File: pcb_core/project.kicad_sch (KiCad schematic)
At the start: 53 parts, among them IC4 TCA9548APWR, J1 Conn_01x02, J19 Conn_02x02_Counter_Clockwise, J2 1725656, J20 PCBConnector, J21 PCBConnector, J22 PCBConnector, J23 PCBConnector, J25 PCBConnector, J27 PCBConnector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

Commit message: Add missing PWR_FLAGs
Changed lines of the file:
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@@
 	)
 	(junction
+		(at 405.13 387.35)
+		(diameter 0)
+		(color 0 0 0 0)
+	)
+	(junction
 		(at 102.87 25.4)
 		(diameter 0)
@@
 	)
 	(junction
+		(at 405.13 389.89)
+		(diameter 0)
+		(color 0 0 0 0)
+	)
+	(junction
 		(at 143.51 349.25)
 		(diameter 0)
@@
 	(wire
 		(pts
+			(xy 405.13 389.89) (xy 414.02 389.89)
+		)
+		(stroke
+			(width 0)
+			(type default)
+		)
+	)
+	(wire
+		(pts
 			(xy 386.08 365.76) (xy 382.27 365.76)
 		)
@@
 	(wire
 		(pts
-			(xy 397.51 389.89) (xy 414.02 389.89)
+			(xy 397.51 389.89) (xy 405.13 389.89)
 		)
 		(stroke
@@
 	(wire
 		(pts
+			(xy 405.13 387.35) (xy 414.02 387.35)
+		)
+		(stroke
+			(width 0)
+			(type default)
+		)
+	)
+	(wire
+		(pts
 			(xy 176.53 116.84) (xy 176.53 118.11)
 		)
@@
 	(wire
 		(pts
-			(xy 383.54 387.35) (xy 414.02 387.35)
+			(xy 383.54 387.35) (xy 405.13 387.35)
 		)
 		(stroke
@@
 		)
 	)
-	(label "VDD33"
-		(at 180.34 31.75 0)
-		(fields_autoplaced yes)
-		(effects
-			(font
-				(size 1.27 1.27)
-			)
-			(justify left bottom)
-		)
-	)
 	(label "ESP32_TX"
 		(at 167.64 45.72 0)
@@
 	)
 	(symbol
+		(lib_id "power:PWR_FLAG")
+		(at 405.13 387.35 0)
+		(unit 1)
+		(exclude_from_sim no)
+		(in_bom yes)
+		(on_board yes)
+		(dnp no)
+		(fields_autoplaced yes)
+		(property "Reference" "#FLG01"
+			(at 405.13 385.445 0)
+			(effects
+				(font
+					(size 1.27 1.27)
+				)
+				(hide yes)
+			)
+		)
+		(property "Value" "PWR_FLAG"
+			(at 405.13 382.27 0)
+			(effects
+				(font
+					(size 1.27 1.27)
+				)
+			)
+		)
+		(property "Footprint" ""
+			(at 405.13 387.35 0)
+			(effects
+				(font
+					(size 1.27 1.27)
+				)
+				(hide yes)
+			)
+		)
+		(property "Datasheet" "~"
+			(at 405.13 387.35 0)
+			(effects
+				(font
+					(size 1.27 1.27)
+				)
+				(hide yes)
+			)
+		)
+		(property "Description" "Special symbol for telling ERC where power comes from"
+			(at 405.13 387.35 0)
+			(effects
+				(font
+					(size 1.27 1.27)
+				)
+				(hide yes)
+			)
+		)
+		(pin "1"
+		)
+		(instances
+			(project "project"
+				(path "/97ee99f6-6664-45d1-b5d6-247aaf34e934"
+					(reference "#FLG01")
+					(unit 1)
+				)
+			)
+		)
+	)
+	(symbol
 		(lib_id "Device:C_Polarized")
 		(at 386.08 361.95 0)
@@
 					(unit 1)
 				)
+			)
+		)
+	)
+	(symbol
+		(lib_id "power:PWR_FLAG")
+		(at 405.13 389.89 180)
+		(unit 1)
+		(exclude_from_sim no)
+		(in_bom yes)
+		(on_board yes)
+		(dnp no)
+		(fields_autoplaced yes)
+		(property "Reference" "#FLG02"
+			(at 405.13 391.795 0)
+			(effects
+				(font
+					(size 1.27 1.27)
+				)
+				(hide yes)
+			)
+		)
+		(property "Value" "PWR_FLAG"
+			(at 405.13 394.97 0)
+			(effects
+				(font
+					(size 1.27 1.27)
+				)
+			)
+		)
+		(property "Footprint" ""
+			(at 405.13 389.89 0)
+			(effects
+				(font
+					(size 1.27 1.27)
+				)
+				(hide yes)
+			)
+		)
+		(property "Datasheet" "~"
+			(at 405.13 389.89 0)
+			(effects
+				(font
+					(size 1.27 1.27)
+				)
+				(hide yes)
+			)
+		)
+		(property "Description" "Special symbol for telling ERC where power comes from"
+			(at 405.13 389.89 0)
+			(effects
+				(font
+					(size 1.27 1.27)
+				)
+				(hide yes)
+			)
+		)
+		(pin "1"
+		)
+		(instances
+			(project "project"
+				(path "/97ee99f6-6664-45d1-b5d6-247aaf34e934"
+					(reference "#FLG02")
+					(unit 1)
+				)

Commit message: Correct BOM values
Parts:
- D1: Mouser Part Number 512-1N4148WT -> 512-1N4148WT
- S1, S2: LCSC# C6191939 -> C6191939
- U1: Manufacturer_Name Espressif Systems -> Espressif Systems
- U2: Manufacturer_Part_Number LTC4365CTS8#TRMPBF -> LTC4365CTS8#TRMPBF
- U3: Manufacturer_Name Espressif Systems -> Espressif Systems; Manufacturer_Part_Number ESP32-DevKitC -> ESP32-DevKitC
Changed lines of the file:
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@@
 			)
 		)
-		(property "Manufacturer_Part_Number" " LTC4365CTS8#TRMPBF"
+		(property "Manufacturer_Part_Number" "LTC4365CTS8#TRMPBF"
 			(at 143.51 365.76 0)
 			(effects
@@
 			)
 		)
-		(property "LCSC#" " C6191939"
+		(property "LCSC#" "C6191939"
 			(at 214.63 22.86 0)
 			(effects
@@
 			)
 		)
-		(property "Manufacturer_Name" " Espressif Systems "
+		(property "Manufacturer_Name" "Espressif Systems "
 			(at 120.65 81.28 0)
 			(effects
@@
 			)
 		)
-		(property "Manufacturer_Name" " Espressif Systems "
+		(property "Manufacturer_Name" "Espressif Systems "
 			(at 335.28 97.79 0)
 			(effects
@@
 			)
 		)
-		(property "Manufacturer_Part_Number" " ESP32-DevKitC "
+		(property "Manufacturer_Part_Number" "ESP32-DevKitC "
 			(at 335.28 97.79 0)
 			(effects
@@
 			)
 		)
-		(property "Mouser Part Number" "512-1N4148WT "
+		(property "Mouser Part Number" "512-1N4148WT"
 			(at 100.33 369.57 0)
 			(effects
@@
 			)
 		)
-		(property "LCSC#" " C6191939"
+		(property "LCSC#" "C6191939"
 			(at 269.24 21.59 0)
 			(effects

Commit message: Correct ERC errors
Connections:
- net +3.3V renamed VCC_3V3

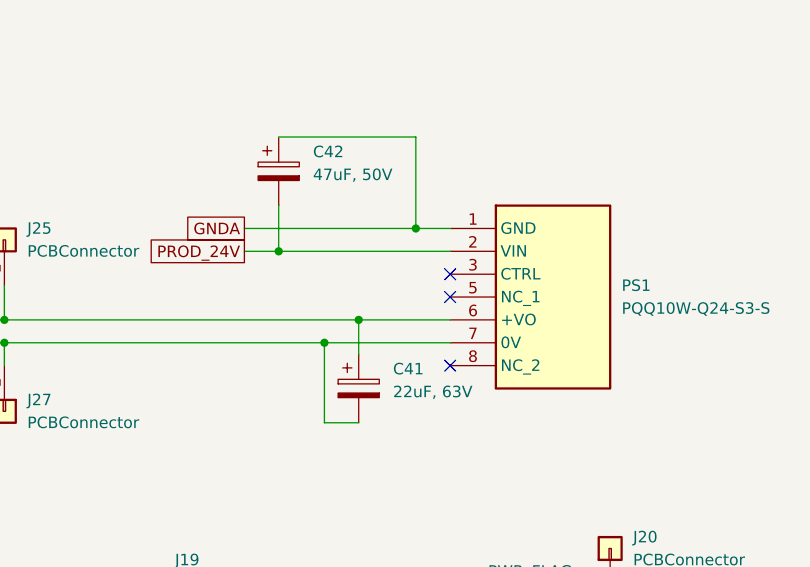
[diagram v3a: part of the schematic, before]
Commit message: Correct BOM errors
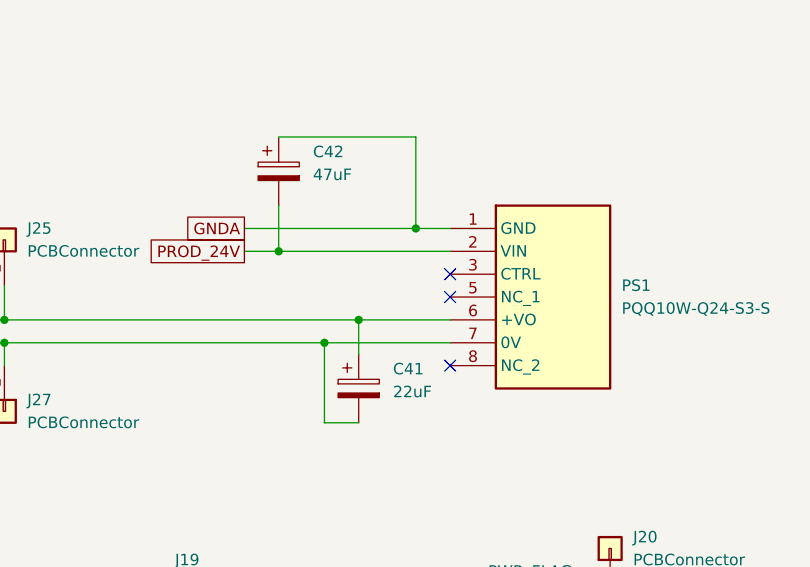
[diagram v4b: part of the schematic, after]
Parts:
- C41: value 22uF, 63V -> 22uF
- C42: value 47uF, 50V -> 47uF
- D1: Manufacturer_Part_Number 1N4148WT -> 1N4148WT
- U1: Manufacturer_Name Espressif Systems -> Espressif Systems; Mouser Part Number 356-ESP3S3WRM2N32R8V -> 356-ESP3S3WRM2N32R8V
- U3: Manufacturer_Name Espressif Systems -> Espressif Systems; Manufacturer_Part_Number ESP32-DevKitC -> ESP32-DevKitC; Mouser Part Number 356-ESP32-DEVKITC -> 356-ESP32-DEVKITC
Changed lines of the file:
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@@
 			)
 		)
-		(property "Value" "22uF, 63V"
+		(property "Value" "22uF"
 			(at 389.89 362.3309 0)
 			(effects
@@
 			)
 		)
-		(property "Manufacturer_Name" "Espressif Systems "
+		(property "Manufacturer_Name" "Espressif Systems"
 			(at 120.65 81.28 0)
 			(effects
@@
 			)
 		)
-		(property "Mouser Part Number" "356-ESP3S3WRM2N32R8V "
+		(property "Mouser Part Number" "356-ESP3S3WRM2N32R8V"
 			(at 120.65 81.28 0)
 			(effects
@@
 			)
 		)
-		(property "Manufacturer_Name" "Espressif Systems "
+		(property "Manufacturer_Name" "Espressif Systems"
 			(at 335.28 97.79 0)
 			(effects
@@
 			)
 		)
-		(property "Manufacturer_Part_Number" "ESP32-DevKitC "
+		(property "Manufacturer_Part_Number" "ESP32-DevKitC"
 			(at 335.28 97.79 0)
 			(effects
@@
 			)
 		)
-		(property "Mouser Part Number" "356-ESP32-DEVKITC "
+		(property "Mouser Part Number" "356-ESP32-DEVKITC"
 			(at 335.28 97.79 0)
 			(effects
@@
 			)
 		)
-		(property "Value" "47uF, 50V"
+		(property "Value" "47uF"
 			(at 381 338.2009 0)
 			(effects
@@
 			)
 		)
-		(property "Manufacturer_Part_Number" "1N4148WT "
+		(property "Manufacturer_Part_Number" "1N4148WT"
 			(at 100.33 369.57 0)
 			(effects
